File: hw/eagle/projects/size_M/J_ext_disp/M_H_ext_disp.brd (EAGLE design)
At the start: 6 parts

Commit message: pcb M.1 -not finished
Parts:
- removed H.D1: RGB_WW-FCE50TC-Q1, hugo:RGB_WW-FCE50TC-Q1
- removed H.J2: (no value), pinhead2:1X06
- removed H.J3: (no value), pinhead2:1X05
- removed H.R1, H.R2, H.R3: 82, resistor:R0603
- added C1, C4: 1u, rcl:C0603
- added C2, C5: 2u2, rcl:C0603
- added C3: 2u, rcl:C0603
- added C6: 100n, rcl:C0603
- added J1: SSD_1306_STM32_OLED, hugo:SSD_1306_STM32_OLED
- added JP1: (no value), pinhead2:1X03
- added JP2: (no value), pinhead2:1X02
- added R1: 390, rcl:R0603
- added R2: 100k, rcl:R0603
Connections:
- removed net N$2: H.D1.3, H.R3.2
- removed net N$4: H.J2.5, H.R1.1
- removed net N$6: H.J2.3, H.R3.1
- new net N$10: C4.1, J1.P$5
- new net N$7: C1.2, J1.P$2
- new net N$8: C1.1, J1.P$3
- new net N$9: C4.2, J1.P$4
- new net PA7: J1.P$13, JP1.3, R2.1
- new net SCL: J1.P$16, JP1.1
- new net SDA: J1.P$17, J1.P$18, JP1.2
- net GND: now also C2.1, C3.1, C5.1, C6.1, J1.P$1, J1.P$10, J1.P$11, J1.P$14, J1.P$15, J1.P$19, J1.P$20, J1.P$21, J1.P$22, J1.P$23, J1.P$27, J1.P$28, J1.P$7, JP2.2, R1.1; no longer H.D1.4, H.D1.5, H.D1.6, H.J2.6, H.J3.4
- net N$1: now also J1.P$24, R1.2; no longer H.D1.1, H.R1.2
- net N$3: now also C3.2, J1.P$26; no longer H.D1.2, H.R2.2
- net N$5: now also C2.2, J1.P$25; no longer H.J2.4, H.R2.1
- net VDD: now also C5.2, C6.2, J1.P$12, J1.P$6, J1.P$8, J1.P$9, JP2.1, R2.2; no longer H.J3.3
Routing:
- net GND: track 33.0 -> 70.9 mm, vias 0 -> 2
- net VDD: track 0.00 -> 26.4 mm
- net PA7: track 0.00 -> 13.1 mm, vias 0 -> 1
- net SCL: track 0.00 -> 12.4 mm, vias 0 -> 1
- net SDA: track 0.00 -> 10.8 mm, vias 0 -> 1
- net N$7: track 0.00 -> 7.82 mm
- net N$9: track 0.00 -> 7.81 mm
- net N$10: track 0.00 -> 5.44 mm
- net N$8: track 0.00 -> 5.09 mm
- net N$4: track 3.25 -> 0.00 mm
- net N$6: track 3.22 -> 0.00 mm
- net N$2: track 3.05 -> 0.00 mm
- net N$5: track 3.05 -> 5.60 mm
- net N$1: track 8.72 -> 6.73 mm
- net N$3: track 6.26 -> 4.95 mm
- added copper zone on layer 16, net GND
- removed copper zone on layer 16, net VDD
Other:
- board text added: "disp M.1"
- board text removed: "RGB M.1"

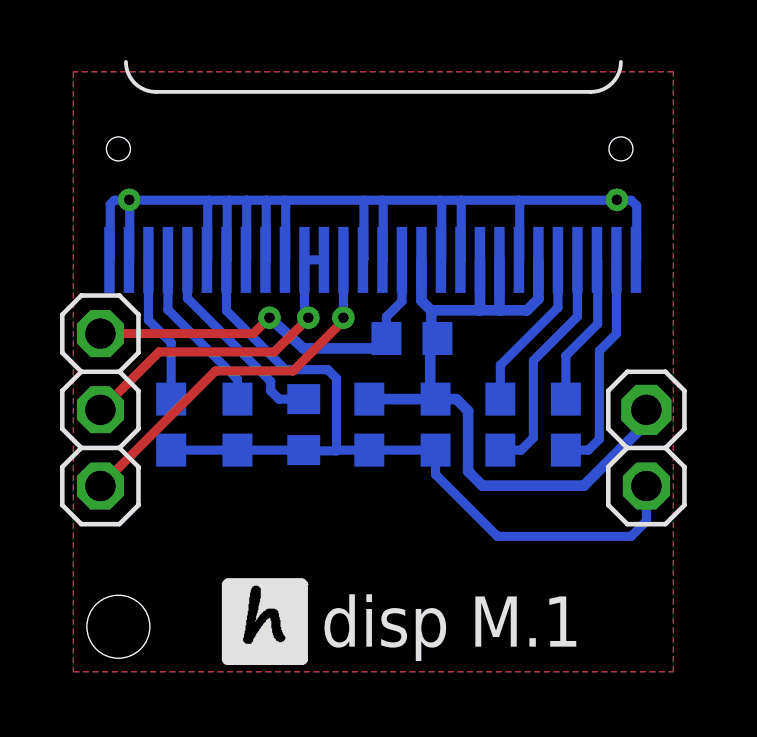
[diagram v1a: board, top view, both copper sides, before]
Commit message: updateed PCBs - adjustments based on usage of version 1
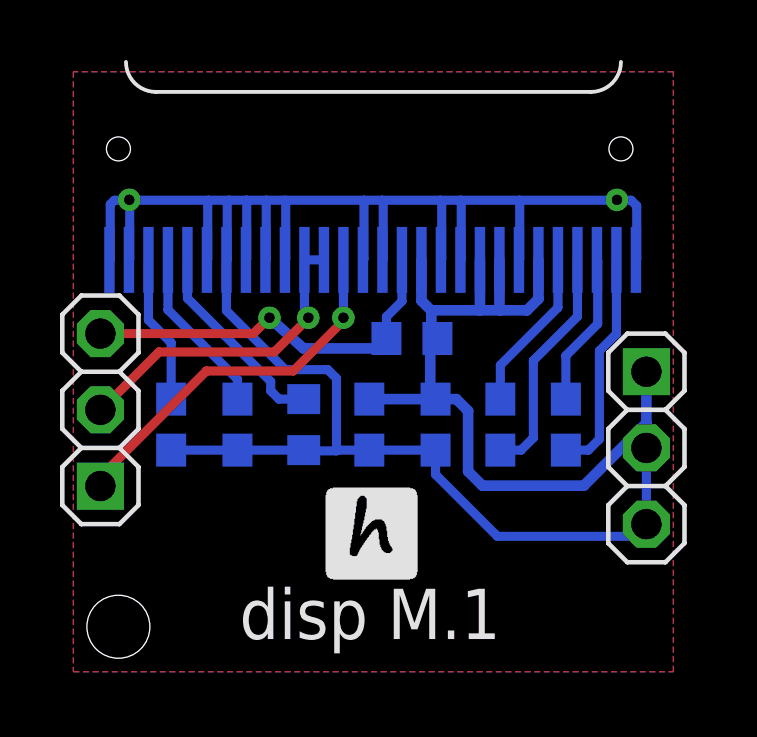
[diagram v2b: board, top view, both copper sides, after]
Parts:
- JP2: device pinhead2:1X02 -> pinhead2:1X03
- renumbered C1 to H.C1, C2 to H.C2, C3 to H.C3, C4 to H.C4, C5 to H.C5, C6 to H.C6, R1 to H.R1, R2 to H.R2
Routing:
- net GND: track 70.9 -> 72.2 mm
- net VDD: track 26.4 -> 27.6 mm
